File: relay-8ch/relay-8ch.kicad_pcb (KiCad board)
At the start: 2 copper layers, 160 x 100 mm, 66 parts, among them J101 Screw_Terminal_01x16, J201 Backplane, K101 G5V-2, K102 G5V-2, K103 G5V-2, K104 G5V-2, K105 G5V-2, K106 G5V-2, K107 G5V-2, K108 G5V-2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

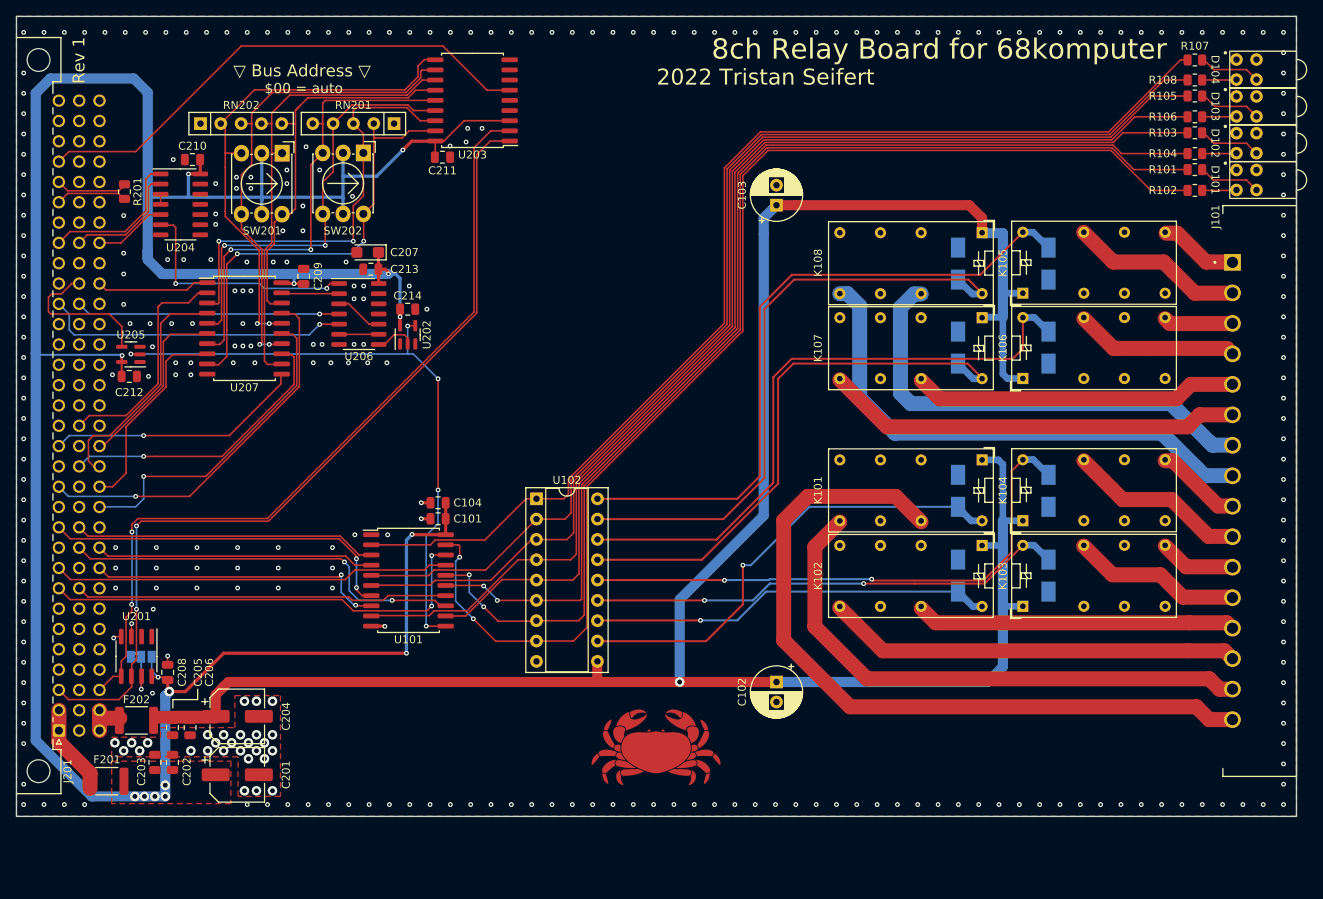
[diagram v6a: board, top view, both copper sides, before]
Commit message: Add backplane breakout; manufacturing tweaks
- Started work on a breakout board for backplane signals; it will slot
  in like a regular expansion card but instead expose all signals on pin
  headers for logic analyzer connection

- Minor tweaks to most boards for manufacturing (mostly adding the
  JLCPCB panel id text placeholders)
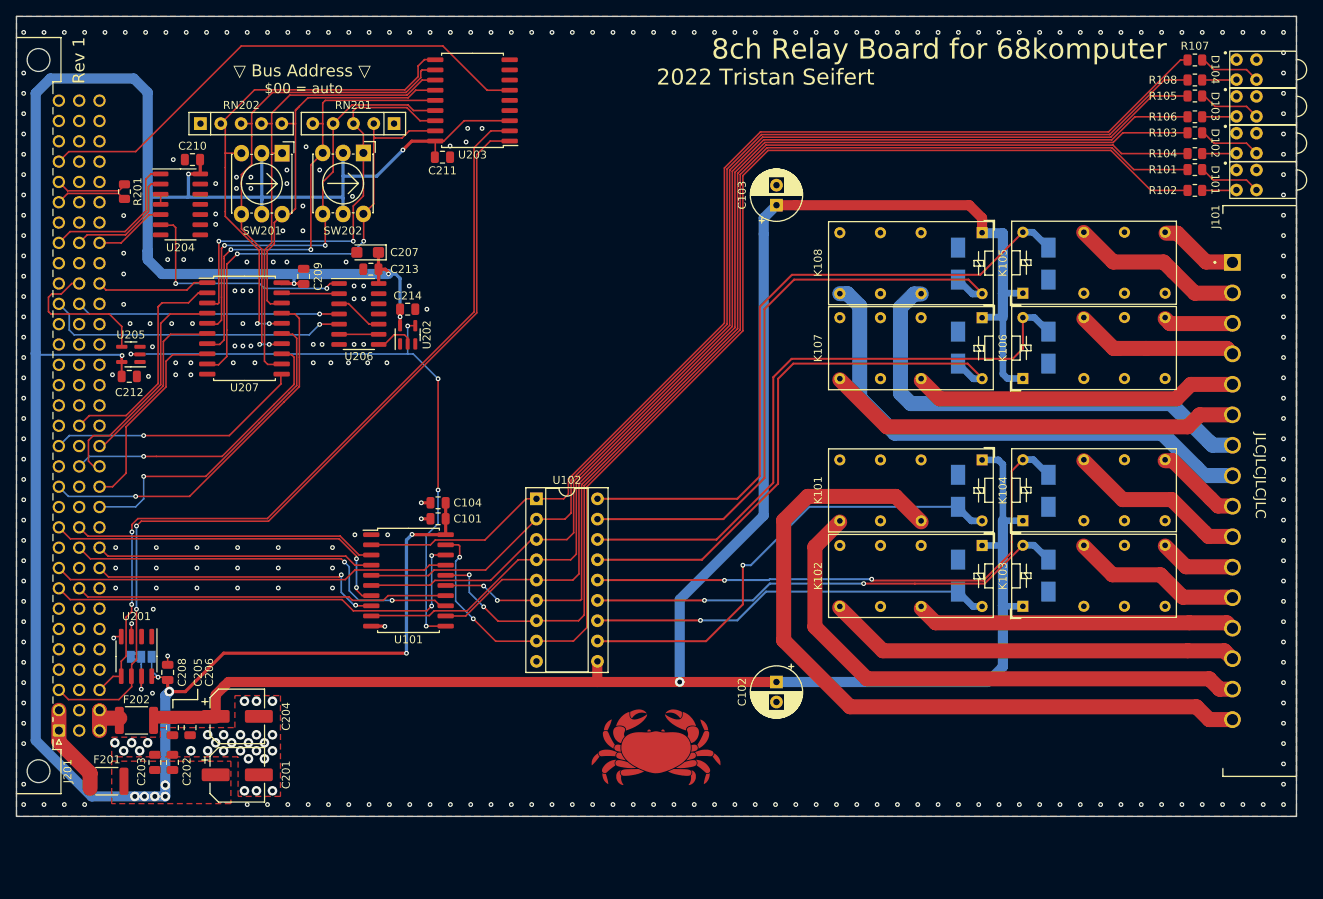
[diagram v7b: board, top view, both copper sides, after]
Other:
- board text added: "JLCJLCJLCJLC"

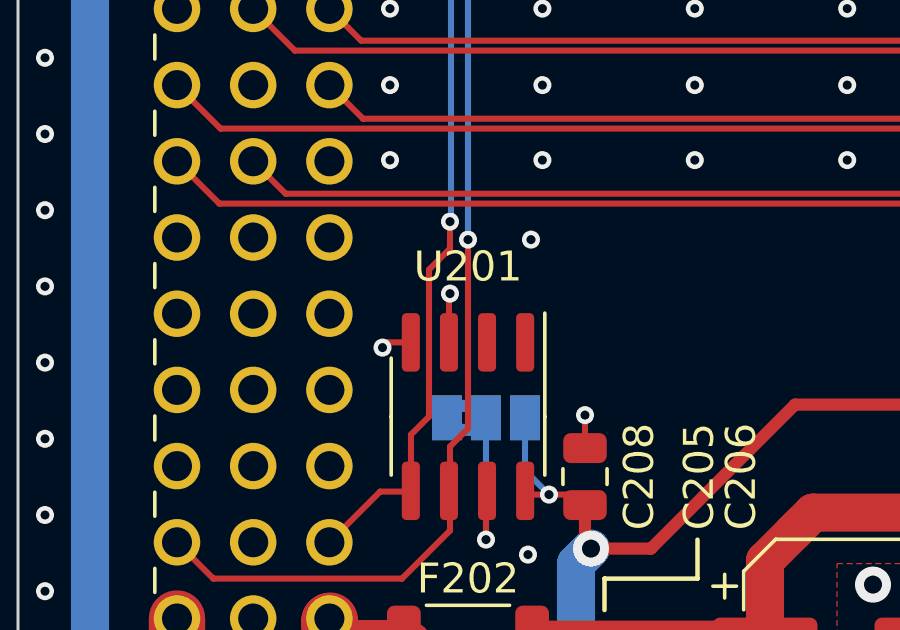
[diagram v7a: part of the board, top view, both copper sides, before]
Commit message: Minor tweaks based from assembly
- Replaced the AT24CS32 EEPROMs with the AT24CS16 which is what was
  ordered. These are half the size, but use a totally different
  addressing scheme which needs to be followed. So, we should just
  standardize on these.

  The information stored in the actual EEPROM section (2KBytes in this
  part) will likely not be much larger than a small 32 byte (or so)
  header.

- Removed a few redundant parts on the power management board, namely
  some resistors

- Fixed the fucked footprint for the PTH08T220WAD module; the annular
  rings were way too small
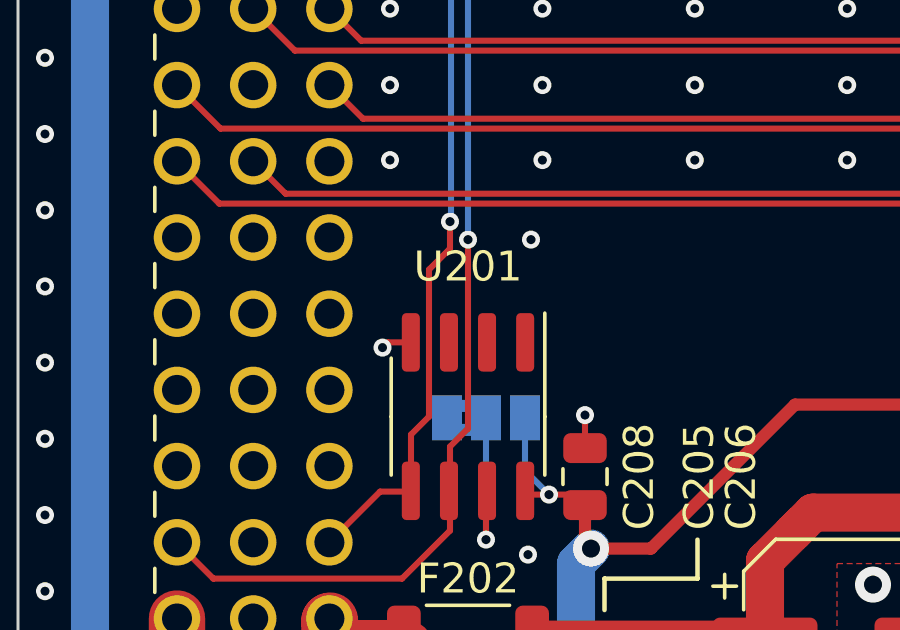
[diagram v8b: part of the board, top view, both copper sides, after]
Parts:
- U201: value AT24CS32-SSHM -> AT24CS16-SSHM
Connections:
- U201 pad 1: GND -> (no net)
- U201 pad 2: GND -> (no net)
- U201 pad 3: GND -> (no net)
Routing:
- net GND: track 7.77 -> 6.13 mm, vias 313 -> 312
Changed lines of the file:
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@@
       (effects (font (size 1 1) (thickness 0.15)))
     )
-    (fp_text value "AT24CS32-SSHM" (at 0 -4.8 -270) (layer "F.Fab")
+    (fp_text value "AT24CS16-SSHM" (at 0 -4.8 -270) (layer "F.Fab")
       (effects (font (size 1 1) (thickness 0.15)))
     )
@@
     (fp_line (start -1.95 2.45) (end -1.95 -1.475) (layer "F.Fab") (width 0.1))
     (fp_line (start -0.975 -2.45) (end 1.95 -2.45) (layer "F.Fab") (width 0.1))
-    (pad "1" smd roundrect locked (at -2.475 -1.905 270) (size 1.95 0.6) (layers "F.Cu" "F.Paste" "F.Mask") (roundrect_rratio 0.25)
-      (net 2 "GND") (pinfunction "A0") (pintype "input"))
-    (pad "2" smd roundrect locked (at -2.475 -0.635 270) (size 1.95 0.6) (layers "F.Cu" "F.Paste" "F.Mask") (roundrect_rratio 0.25)
-      (net 2 "GND") (pinfunction "A1") (pintype "input"))
-    (pad "3" smd roundrect locked (at -2.475 0.635 270) (size 1.95 0.6) (layers "F.Cu" "F.Paste" "F.Mask") (roundrect_rratio 0.25)
-      (net 2 "GND") (pinfunction "A2") (pintype "input"))
+    (pad "1" smd roundrect locked (at -2.475 -1.905 270) (size 1.95 0.6) (layers "F.Cu" "F.Paste" "F.Mask") (roundrect_rratio 0.25))
+    (pad "2" smd roundrect locked (at -2.475 -0.635 270) (size 1.95 0.6) (layers "F.Cu" "F.Paste" "F.Mask") (roundrect_rratio 0.25))
+    (pad "3" smd roundrect locked (at -2.475 0.635 270) (size 1.95 0.6) (layers "F.Cu" "F.Paste" "F.Mask") (roundrect_rratio 0.25))
     (pad "4" smd roundrect locked (at -2.475 1.905 270) (size 1.95 0.6) (layers "F.Cu" "F.Paste" "F.Mask") (roundrect_rratio 0.25)
       (net 2 "GND") (pinfunction "GND") (pintype "power_in"))
@@
   (segment (start 71.75 82.8) (end 70.6 82.8) (width 0.4064) (layer "F.Cu") (net 2))
   (segment (start 32.325 97.525) (end 33.095 97.525) (width 0.2032) (layer "F.Cu") (net 2))
-  (segment (start 34.365 95.935) (end 34.4 95.9) (width 0.2032) (layer "F.Cu") (net 2))
-  (segment (start 34.365 97.525) (end 34.365 95.935) (width 0.2032) (layer "F.Cu") (net 2))
   (segment (start 32.15 97.7) (end 32.325 97.525) (width 0.2032) (layer "F.Cu") (net 2))
   (segment (start 66.015 96.215) (end 66.05 96.25) (width 0.4064) (layer "F.Cu") (net 2))
@@
   (via (at 175.84 22) (size 0.6) (drill 0.3) (layers "F.Cu" "B.Cu") (free) (net 2))
   (via (at 52.72 86.4) (size 0.6) (drill 0.3) (layers "F.Cu" "B.Cu") (free) (net 2))
-  (via (at 34.4 95.9) (size 0.6) (drill 0.3) (layers "F.Cu" "B.Cu") (free) (net 2))
   (via (at 23.44 22) (size 0.6) (drill 0.3) (layers "F.Cu" "B.Cu") (free) (net 2))
   (via (at 173.3 118.52) (size 0.6) (drill 0.3) (layers "F.Cu" "B.Cu") (free) (net 2))
